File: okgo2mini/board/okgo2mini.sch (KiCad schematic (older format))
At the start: 43 parts

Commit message: switches for okgo2 mini and usb
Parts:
- SW?: Farnell (none) -> 9574743
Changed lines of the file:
@@
 F 1 "SWITCH_SPST" H 3000 5614 50  0000 C CNN
 F 2 "" H 3000 5450 50  0001 C CNN
-F 3 "" H 3000 5450 50  0001 C CNN
+F 3 "http://www.farnell.com/datasheets/19431.pdf" H 3000 5450 50  0001 C CNN
+F 4 "9574743" H 3000 5450 60  0001 C CNN "Farnell"
 	1    3000 5450
 	1    0    0    -1

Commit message: okgo2mini footprints
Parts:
- removed C?: DNF, agg:0603, symbol C
- added C?: 10u, agg:0603, symbol C
- C? (x15), R? (x5): footprint (none) -> agg:0603
- C?: value 22u -> 10u; footprint (none) -> agg:0603
- D?: footprint (none) -> agg:0805-LED; Farnell (none) -> 2079908
- D?: footprint (none) -> agg:0805-LED; symbol LED -> LED-RESCUE-okgo2mini; Farnell (none) -> 2610420
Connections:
- net at C?.1, D?.1, IC?.14 (VOS)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: now also C?.1
- no-connect marks 19 -> 20
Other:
- moved on the sheet: C?, D?, J?, R?

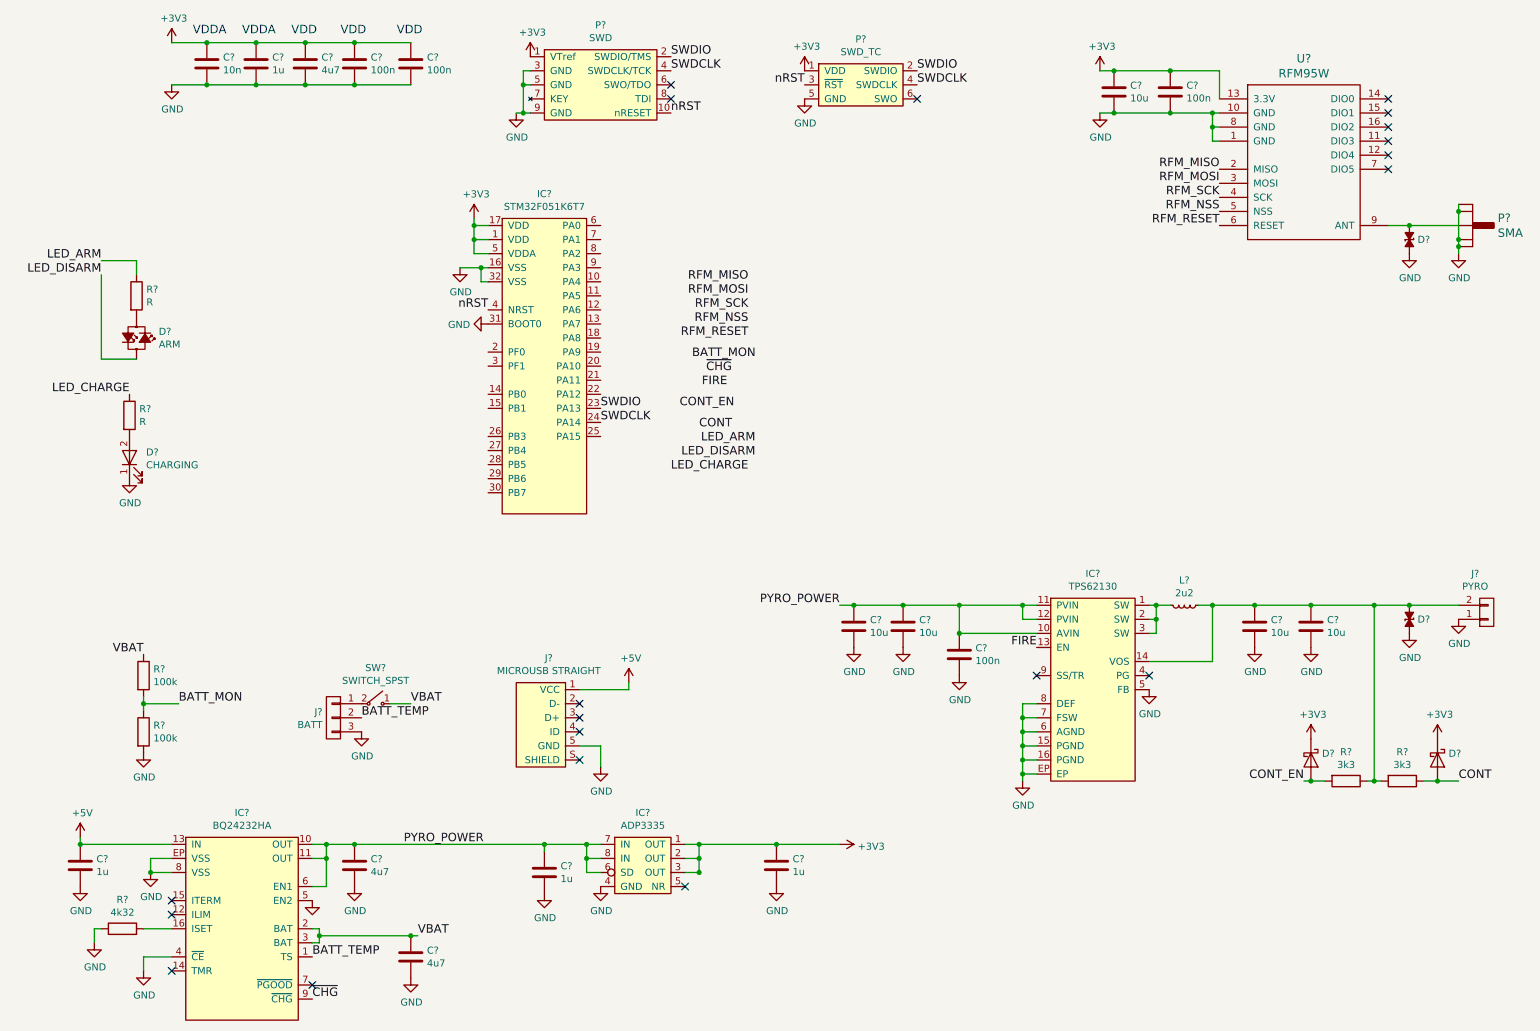
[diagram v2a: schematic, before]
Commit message: footprints for okgo2mini and usbcontrol
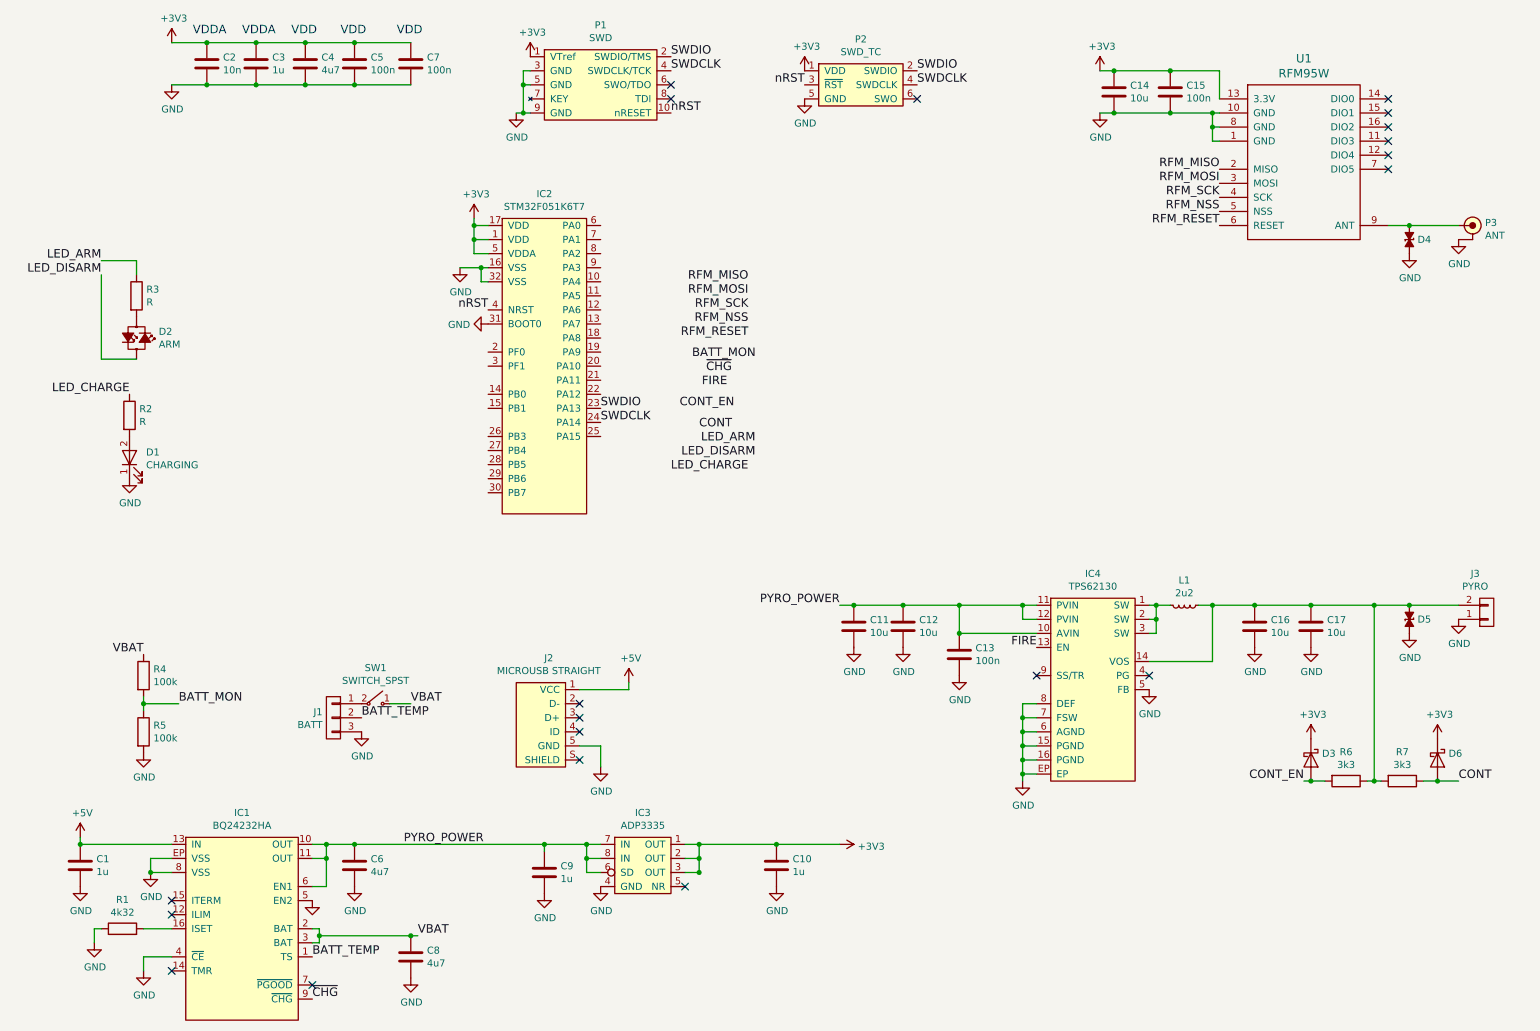
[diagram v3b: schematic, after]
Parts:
- removed P?: SMA, symbol SMA
- added P3: ANT, agg:SMA-EDGE, symbol COAX
- J1: renamed from J?; footprint (none) -> agg:S03B-PASK-2
- J2: renamed from J?; footprint (none) -> okgo2mini:USB_Micro_B_Vertical
- J3: renamed from J?; footprint (none) -> agg:S02B-PASK-2
- R6, R7: renamed from R?; footprint (none) -> agg:0603
- SW1: renamed from SW?; footprint (none) -> okgo2mini:710xxxxV3xx
- U1: renamed from U?; footprint (none) -> okgo2mini:RFM95W
- gave numbers to parts that had none: 35
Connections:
- net GND: now also C17.2, P3.2 (GND)
- net at D4.1, U1.9 (ANT): now also P3.1 (RF)

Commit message: Minified parts, did some order codes
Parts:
- D4, D5: Farnell (none) -> 2368173
- U1: Farnell (none) -> RF00490

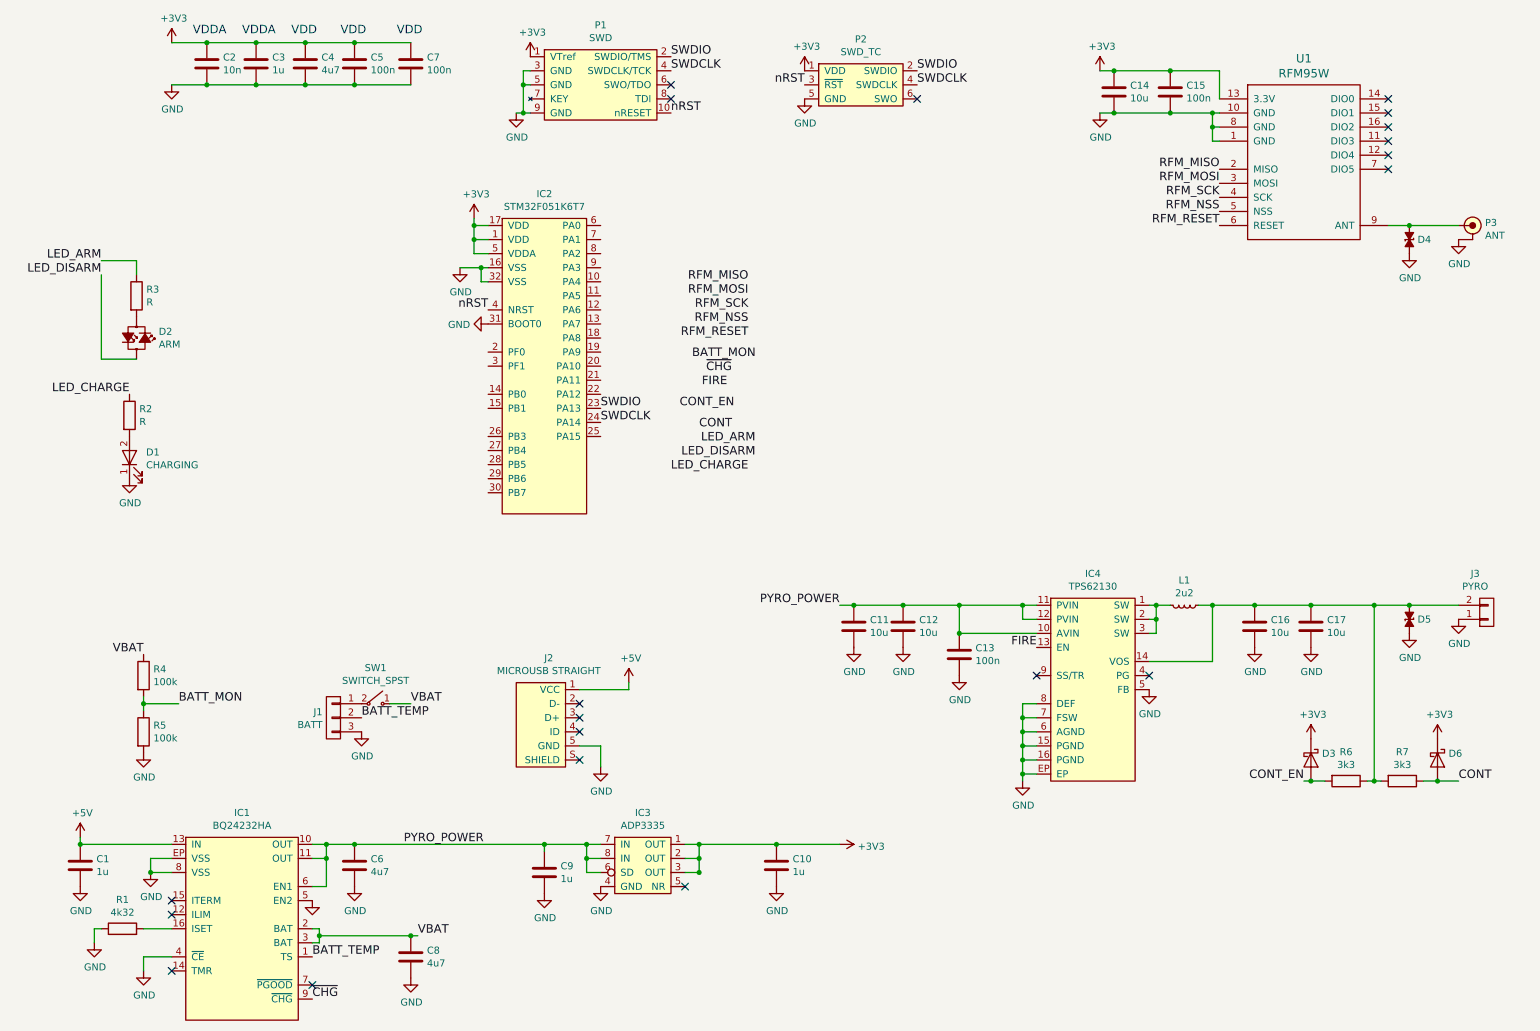
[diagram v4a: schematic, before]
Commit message: Si5515 fire switch, DPDT switch 5V & batt
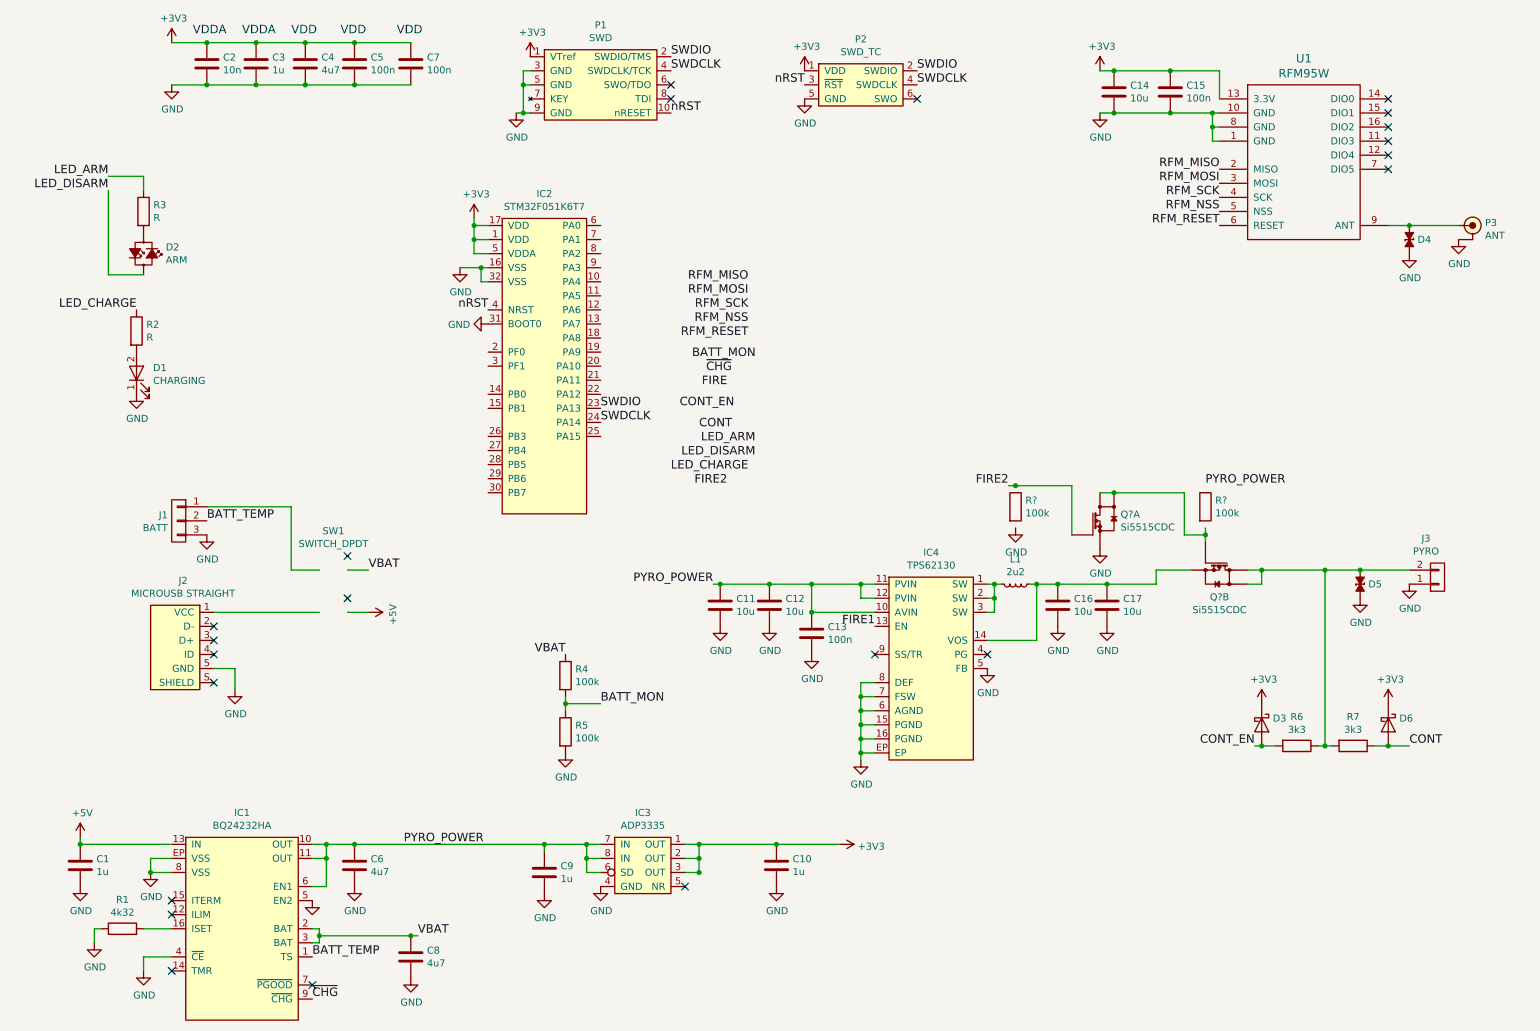
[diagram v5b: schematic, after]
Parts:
- removed SW1: SWITCH_SPST, okgo2mini:710xxxxV3xx, symbol SWITCH_SPST
- added Q? (x2): Si5515CDC, agg:ChipFET-1206-8, symbol Si5515CDC
- added R? (x2): 100k, agg:0603, symbol R
- added SW1: SWITCH_DPDT, okgo2mini:120x-M1-xx-C, symbol SWITCH_DPDT
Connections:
- net labels added: FIRE1, FIRE2
- wire segments 81 -> 95
- no-connect marks 20 -> 22
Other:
- moved on the sheet: C11, C12, C13, C16, C17, D1, D2, D3, D5, D6, IC4, J1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

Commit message: WIP
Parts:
- added P4: u.FL, unchecked:uFL-R-SMT, symbol COAX
- added X1, X2, X3, X4: M3 Mount, agg:M3_MOUNT, symbol PART
- D1, D2: footprint agg:0805-LED -> LEDs:LED_D3.0mm
- P3: value ANT -> SMA
- gave numbers to parts that had none: 3
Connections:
- wire segments 95 -> 100
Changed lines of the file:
@@
 LIBS:contrib
 LIBS:valves
+LIBS:stm32f0xxkxtx
+LIBS:swd
+LIBS:swd_tc
+LIBS:esd_diode
+LIBS:tps62130
+LIBS:adp3335
+LIBS:bq24232ha
+LIBS:microusb
 LIBS:coax
 LIBS:si5515cdc
 LIBS:switch
+LIBS:part
 LIBS:okgo2mini-cache
 EELAYER 26 0
@@
 F 0 "D2" V 1304 2408 50  0000 L CNN
 F 1 "ARM" V 1395 2408 50  0000 L CNN
-F 2 "agg:0805-LED" V 1350 2310 60  0001 C CNN
+F 2 "LEDs:LED_D3.0mm" V 1350 2310 60  0001 C CNN
 F 3 "http://onecall.farnell.com/kingbright/kpb-2012surkcgkc/led-smd-bi-polar-0805-red-green/dp/2079908" V 1350 2310 60  0001 C CNN
 F 4 "2079908" H 1350 2250 60  0001 C CNN "Farnell"
@@
 F 0 "D1" V 1338 2982 50  0000 R CNN
 F 1 "CHARGING" V 1247 2982 50  0000 R CNN
-F 2 "agg:0805-LED" H 1300 3100 50  0001 C CNN
+F 2 "LEDs:LED_D3.0mm" H 1300 3100 50  0001 C CNN
 F 3 "http://www.farnell.com/datasheets/2068434.pdf" H 1300 3100 50  0001 C CNN
 F 4 "2610420" H 1300 3100 60  0001 C CNN "Farnell"
@@
 Text Label 1800 4150 0    60   ~ 0
 BATT_TEMP
-Text Label 2950 4500 0    60   ~ 0
+Text Label 2950 4400 0    60   ~ 0
 VBAT
 Text Label 4350 5100 2    60   ~ 0
@@
 L +5V #PWR06
 U 1 1 59976218
-P 2950 4800
-F 0 "#PWR06" H 2950 4650 50  0001 C CNN
-F 1 "+5V" H 2965 4973 50  0000 C CNN
-F 2 "" H 2950 4800 50  0001 C CNN
-F 3 "" H 2950 4800 50  0001 C CNN
-	1    2950 4800
+P 2950 4700
+F 0 "#PWR06" H 2950 4550 50  0001 C CNN
+F 1 "+5V" H 2965 4873 50  0000 C CNN
+F 2 "" H 2950 4700 50  0001 C CNN
+F 3 "" H 2950 4700 50  0001 C CNN
+	1    2950 4700
 	0    1    1    0
 $EndComp
@@
 L GND #PWR028
 U 1 1 5998B464
-P 10700 2150
-F 0 "#PWR028" H 10700 1900 50  0001 C CNN
-F 1 "GND" H 10705 1977 50  0000 C CNN
-F 2 "" H 10700 2150 50  0001 C CNN
-F 3 "" H 10700 2150 50  0001 C CNN
-	1    10700 2150
+P 10650 2150
+F 0 "#PWR028" H 10650 1900 50  0001 C CNN
+F 1 "GND" H 10655 1977 50  0000 C CNN
+F 2 "" H 10650 2150 50  0001 C CNN
+F 3 "" H 10650 2150 50  0001 C CNN
+	1    10650 2150
 	1    0    0    -1
 $EndComp
@@
 P 10800 2050
 F 0 "P3" H 10888 2070 50  0000 L CNN
-F 1 "ANT" H 10888 1979 50  0000 L CNN
+F 1 "SMA" H 10888 1979 50  0000 L CNN
 F 2 "agg:SMA-EDGE" H 10800 1840 50  0001 C CNN
 F 3 "" H 10900 1950 50  0001 C CNN
@@
 $EndComp
 $Comp
-L Si5515CDC Q?
+L Si5515CDC Q1
 U 1 1 5999B957
 P 8150 4150
-F 0 "Q?" H 8297 4196 50  0000 L CNN
+F 0 "Q1" H 8297 4196 50  0000 L CNN
 F 1 "Si5515CDC" H 8297 4105 50  0000 L CNN
 F 2 "agg:ChipFET-1206-8" H 8150 3400 50  0001 C CNN
@@
 $EndComp
 $Comp
-L Si5515CDC Q?
+L Si5515CDC Q1
 U 2 1 5999BC82
 P 9000 4500
-F 0 "Q?" V 9192 4500 50  0000 C CNN
+F 0 "Q1" V 9192 4500 50  0000 C CNN
 F 1 "Si5515CDC" V 9283 4500 50  0000 C CNN
 F 2 "agg:ChipFET-1206-8" H 9000 3750 50  0001 C CNN
@@
 	8800 4500 8550 4500
 Wire Wire Line
-	8550 4500 8550 4600
-$Comp
-L R R?
-U 0 1 599A3C5A
+	8550 4600 8550 4500
+$Comp
+L R R9
+U 1 1 599A3C5A
 P 8900 4050
-F 0 "R?" H 8970 4096 50  0000 L CNN
+F 0 "R9" H 8970 4096 50  0000 L CNN
 F 1 "100k" H 8970 4005 50  0000 L CNN
 F 2 "agg:0603" V 8830 4050 50  0001 C CNN
 F 3 "" H 8900 4050 50  0000 C CNN
-	0    8900 4050
+	1    8900 4050
 	1    0    0    -1
 $EndComp
@@
 	8900 4200 8900 4300
 $Comp
-L GND #PWR?
-U 0 1 599A400F
+L GND #PWR042
+U 1 1 599A400F
 P 8150 4350
-F 0 "#PWR?" H 8150 4100 50  0001 C CNN
+F 0 "#PWR042" H 8150 4100 50  0001 C CNN
 F 1 "GND" H 8155 4177 50  0000 C CNN
 F 2 "" H 8150 4350 50  0000 C CNN
 F 3 "" H 8150 4350 50  0000 C CNN
-	0    8150 4350
+	1    8150 4350
 	1    0    0    -1
 $EndComp
@@
 FIRE2
 $Comp
-L R R?
-U 0 1 599A50E2
+L R R8
+U 1 1 599A50E2
 P 7550 4050
-F 0 "R?" H 7620 4096 50  0000 L CNN
+F 0 "R8" H 7620 4096 50  0000 L CNN
 F 1 "100k" H 7620 4005 50  0000 L CNN
 F 2 "agg:0603" H 7620 3959 50  0001 L CNN
 F 3 "" H 7550 4050 50  0000 C CNN
-	0    7550 4050
+	1    7550 4050
 	1    0    0    -1
 $EndComp
@@
 	7950 3900 7950 4250
 $Comp
-L GND #PWR?
-U 0 1 599A53A7
+L GND #PWR043
+U 1 1 599A53A7
 P 7550 4200
-F 0 "#PWR?" H 7550 3950 50  0001 C CNN
+F 0 "#PWR043" H 7550 3950 50  0001 C CNN
 F 1 "GND" H 7555 4027 50  0000 C CNN
 F 2 "" H 7550 4200 50  0000 C CNN
 F 3 "" H 7550 4200 50  0000 C CNN
-	0    7550 4200
+	1    7550 4200
 	1    0    0    -1
 $EndComp
@@
 Connection ~ 9300 4500
 Wire Wire Line
-	8550 4600 7650 4600
+	7650 4600 8550 4600
 $Comp
 L SWITCH_DPDT SW1
-U 0 1 599A88CA
+U 1 1 599A88CA
 P 2700 4600
 F 0 "SW1" H 2700 4978 50  0000 C CNN
@@
 F 3 "http://www.farnell.com/datasheets/19431.pdf" H 2700 4600 50  0001 C CNN
 F 4 "9574743" H 2700 4600 60  0001 C CNN "Farnell"
-	0    2700 4600
-	1    0    0    -1
-$EndComp
-NoConn ~ 2800 4400
-Wire Wire Line
-	2800 4500 2950 4500
+	1    2700 4600
+	1    0    0    -1
+$EndComp
+NoConn ~ 2800 4500
+Wire Wire Line
+	2800 4400 2950 4400
 Wire Wire Line
 	1800 4050 2400 4050
@@
 Wire Wire Line
 	2400 4500 2600 4500
-NoConn ~ 2800 4700
-Wire Wire Line
-	2800 4800 2950 4800
+NoConn ~ 2800 4800
+Wire Wire Line
+	2800 4700 2950 4700
+$Comp
+L PART X2
+U 1 1 5999D17C
+P 500 3925
+F 0 "X2" H 550 4000 50  0000 L CNN
+F 1 "M3 Mount" H 550 3925 50  0000 L CNN
+F 2 "agg:M3_MOUNT" H 500 3925 50  0001 C CNN
+F 3 "" H 500 3925 50  0001 C CNN
+	1    500  3925
+	1    0    0    -1
+$EndComp
+$Comp
+L PART X3
+U 1 1 5999D8F7
+P 500 4125
+F 0 "X3" H 550 4200 50  0000 L CNN
+F 1 "M3 Mount" H 550 4125 50  0000 L CNN
+F 2 "agg:M3_MOUNT" H 500 4125 50  0001 C CNN
+F 3 "" H 500 4125 50  0001 C CNN
+	1    500  4125
+	1    0    0    -1
+$EndComp
+$Comp
+L PART X4
+U 1 1 5999D983
+P 500 4325
+F 0 "X4" H 550 4400 50  0000 L CNN
+F 1 "M3 Mount" H 550 4325 50  0000 L CNN
+F 2 "agg:M3_MOUNT" H 500 4325 50  0001 C CNN
+F 3 "" H 500 4325 50  0001 C CNN
+	1    500  4325
+	1    0    0    -1
+$EndComp
+$Comp
+L PART X1
+U 1 1 5999DA0D
+P 500 3725
+F 0 "X1" H 550 3800 50  0000 L CNN
+F 1 "M3 Mount" H 550 3725 50  0000 L CNN
+F 2 "agg:M3_MOUNT" H 500 3725 50  0001 C CNN
+F 3 "" H 500 3725 50  0001 C CNN
+	1    500  3725
+	1    0    0    -1
+$EndComp
+$Comp
+L COAX P4
+U 1 1 5999E18E
+P 10800 1875
+F 0 "P4" H 10888 1895 50  0000 L CNN
+F 1 "u.FL" H 10888 1804 50  0000 L CNN
+F 2 "unchecked:uFL-R-SMT" H 10800 1665 50  0001 C CNN
+F 3 "http://www.farnell.com/datasheets/1947917.pdf?_ga=2.18166704.88153315.1503249420-263041513.1492720065" H 10900 1775 50  0001 C CNN
+F 4 "1688077" H 10800 1595 50  0001 C CNN "Farnell"
+	1    10800 1875
+	1    0    0    -1
+$EndComp
+Wire Wire Line
+	10700 1875 10575 1875
+Wire Wire Line
+	10575 1875 10575 2050
+Connection ~ 10575 2050
+Wire Wire Line
+	10700 1975 10650 1975
+Wire Wire Line
+	10650 1975 10650 2150
+Wire Wire Line
+	10650 2150 10700 2150
+Connection ~ 10650 2150
 $EndSCHEMATC
